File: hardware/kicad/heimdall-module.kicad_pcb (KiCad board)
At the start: 2 copper layers, 54.9 x 30.1 mm, 28 parts

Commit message: Sync the imported PCB with the schematic and clean up ERC
After Update PCB from Schematic, the pads were on the new hierarchical
nets (/VCC, /SDA, ...) but tracks, vias and zones kept the old names;
moved them over. Removed EasyEDA's A4 frame symbol and empty Field42
properties. Gave pins real types: passives, connectors and diode are
passive, MC33269 Vin/Vout are power in/out, ESP32 IOs bidirectional.
GND is now a KiCad power symbol. ERC is down from 100 to 19 and DRC from
167 to 92; what is left is design and layout, not import.

Co-Authored-By: Claude Opus 5.5 <noreply@anthropic.com>
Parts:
- C1: value (none) -> 330nF
- C2: value (none) -> 10uF
- C3, C4: value (none) -> 100nF
- D1: value (none) -> 1N5819
- H1: value (none) -> BG125-05-A-1-1-0440-N-D
- R1, R2: value (none) -> 5.1kΩ
- R10, R8, R9: value (none) -> 10kΩ
- R3, R4: value (none) -> 33Ω
- R5, R6, R7: value (none) -> 220Ω
- U1: value (none) -> MC33269DT-3.3G
- U2: value (none) -> 2.4GHz
- U3: value (none) -> TYPEC-214-ARP14H105
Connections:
- net $1N100 renamed Net-(U2-EN)
- net $1N29 renamed Net-(U3-CC1)
- net $1N37 renamed Net-(U3-CC2)
- net $1N69 renamed Net-(U2-IO19)
- net $1N70 renamed Net-(U2-IO18)
- net $1N77 renamed Net-(U2-IO4)
- net $1N78 renamed Net-(U2-IO5)
- net $1N81 renamed Net-(U2-IO6)
- net DATA renamed /DATA
- net HB renamed /HB
- net IO10 renamed /IO10
- net IO3 renamed /IO3
- net IO7 renamed /IO7
- net RXD renamed /RXD
- net SCL renamed /SCL
- net SDA renamed /SDA
- net SIGNAL renamed /SIGNAL
- net TXD renamed /TXD
- net USB-D+ renamed /USB-D+
- net USB-D- renamed /USB-D-
- net VBAT renamed /VBAT
- net VBUS renamed /VBUS
- net VCC renamed /VCC
- U2 pad 16: (no net) -> unconnected-(U2-IO2-Pad16)
- U2 pad 7: (no net) -> unconnected-(U2-IO8-Pad7)
- U2 pad 8: (no net) -> unconnected-(U2-IO9-Pad8)

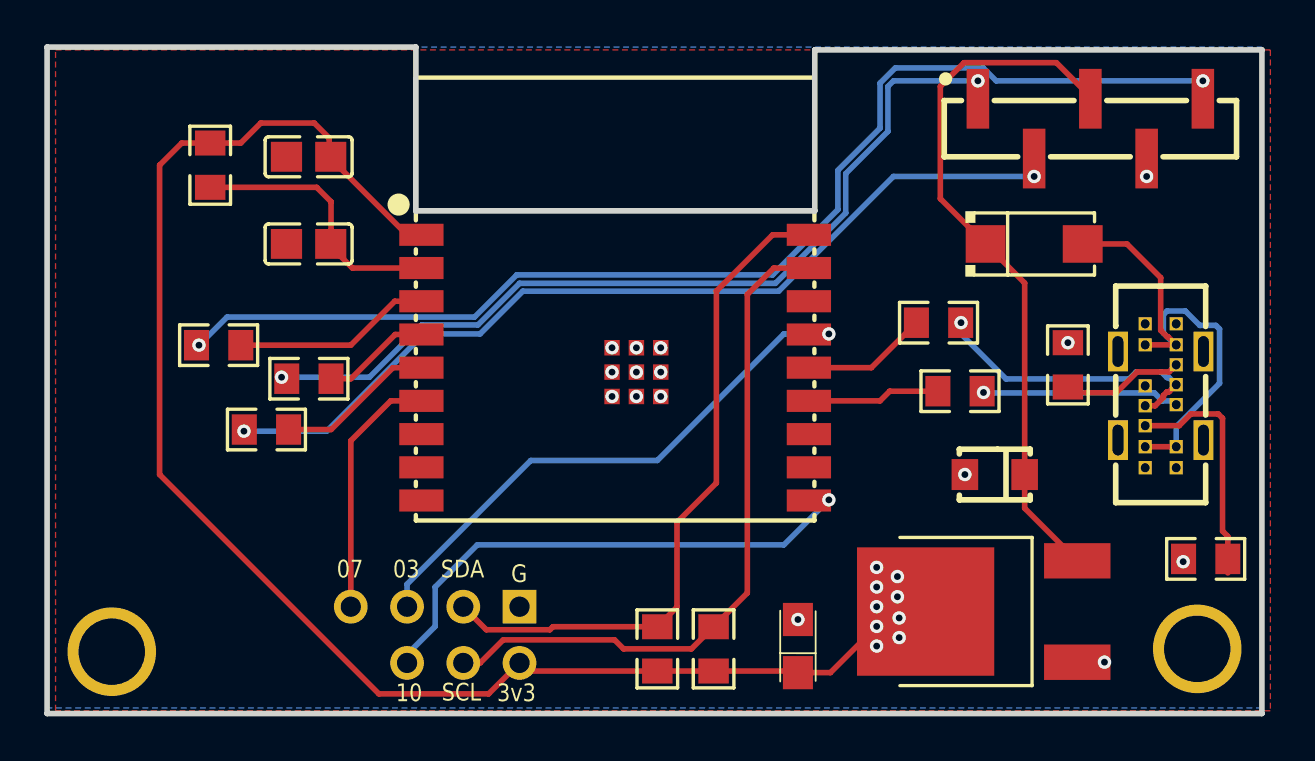
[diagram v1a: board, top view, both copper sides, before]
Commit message: Rev 2: corrected schematic, re-placed and re-routed board
Schematic (on top of the previous commit):
- I2C moved from IO0/IO1 to GPIO20/21 and bay SIGNAL/DATA swapped onto
  IO4/IO5, so the right-hand pins can reach J2 without crossing the 3V3
  trunk. No firmware exists yet. SCL sits on U0TXD (boot log); SDA stays a
  pulled-up input, so no I2C start condition happens at boot. The console
  has to use USB-Serial/JTAG.
- JP1 kept out of BOM/position files; U2 value -> part name.

PCB:
- H1 slot restored: EasyEDA had it as a multi-layer fill (became copper
  in the import). Now a 12.7 x 2.03mm cut-out, H1's pads trimmed to end
  0.5mm before it.
- All copper rebuilt: power class 0.6mm (VBUS, VBAT, VBAT_IN), 3V3 trunk
  0.5mm (Espressif: >= 20 mil), signals 0.25mm, 0.2mm clearance,
  0.7/0.3 and 0.8/0.4 vias. No via touches a pad (checked).
- U1 tab heatsink copper on both layers, vias beside the tab, not in it.
- No tracks/vias on top under the module body (GND only).
- Vertical USB-C: round 0.7mm pads (0.6mm square gave a 0.09mm ring);
  the pin field (VBUS, CC, D+/D- crossover) laid by hand.
- GND pours on both layers, stitched; a GND track along the module's
  bottom pad row joins the right-hand side to the rest.
- Edited footprints written back to the project library.
- route_pcb.py (adapted from heimdall-switch) and rev_pcb.py record how it
  was made.

ERC 0. DRC 0 errors, 0 unconnected, 0 parity; 1 warning (U3 A1 thermal
relief on top has one spoke; the pad also joins the bottom pour).

Co-Authored-By: Claude Opus 5.5 <noreply@anthropic.com>
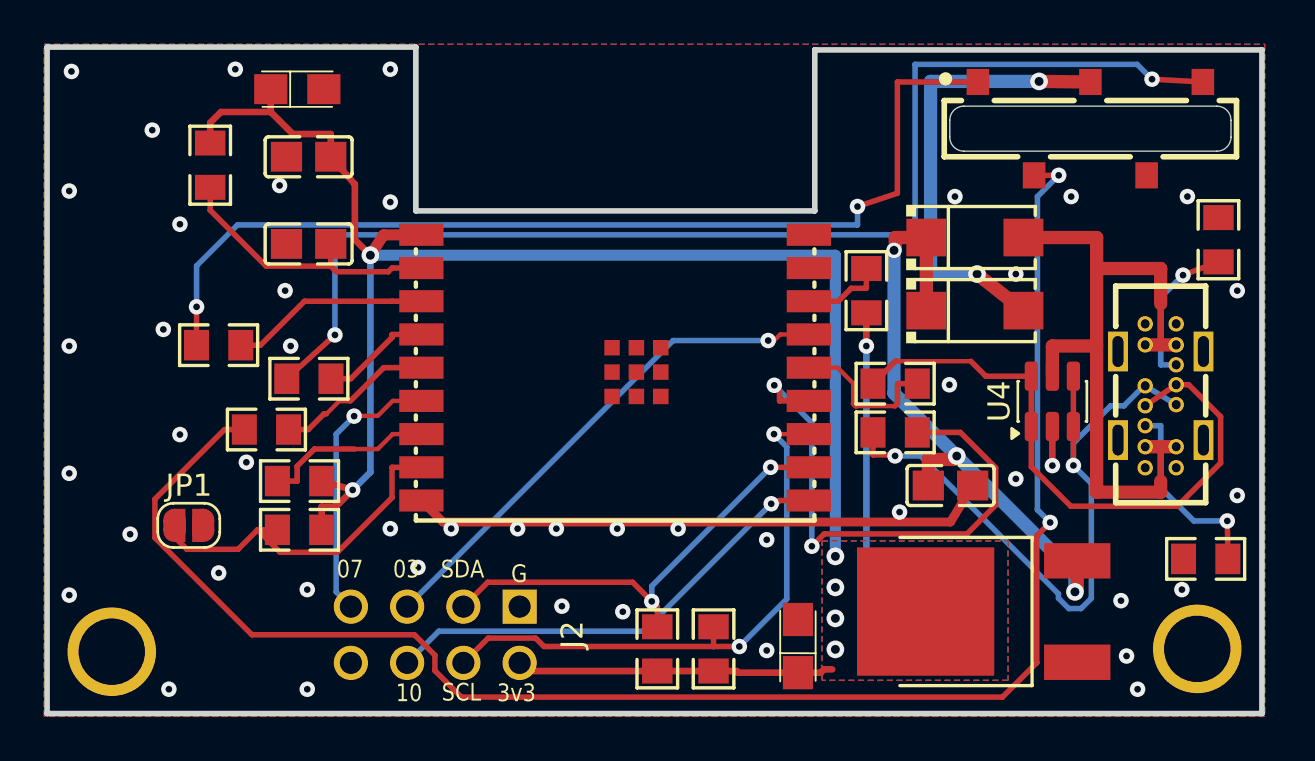
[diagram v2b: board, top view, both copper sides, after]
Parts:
- removed ?: , Pad_e209
- removed ?: , Pad_e211
- removed ?: , Pad_e210
- removed ?: , Pad_e207
- removed ?: , Pad_e206
- removed ?: , Pad_e212
- removed ?: , Pad_e208
- added C5: 10uF, heimdall-m-easyedapro:CASE-A_3216, F.Cu at (131.3, 91.9)
- added D2: 1N5819, heimdall-m-easyedapro:SMA_L4.4-W2.6-LS5.0-RD, F.Cu at (161.9, 101.9)
- added J2: Breakout, Connector_PinHeader_2.54mm:PinHeader_2x04_P2.54mm_Vertical, F.Cu at (141.3, 115.3)
- added JP1: BOOT, Jumper:SolderJumper-2_P1.3mm_Open_RoundedPad1.0x1.5mm, F.Cu at (126.4, 111.6)
- added R11: 10kΩ, heimdall-m-easyedapro:R0805, F.Cu at (157.0, 101.0)
- added R12: 10kΩ, heimdall-m-easyedapro:R0805, F.Cu at (131.4, 109.6)
- added R13: 10kΩ, heimdall-m-easyedapro:R0805, F.Cu at (131.4, 111.8)
- added U4: USBLC6-2SC6, Package_TO_SOT_SMD:SOT-23-6, F.Cu at (165.4, 106.0)
- C1: value 330nF -> 1uF; footprint heimdall-m-easyedapro:CAP-SMD_L3.2-W1.6 -> heimdall-m-easyedapro:C0805
- C4: value 100nF -> 1uF
- U2: value 2.4GHz -> ESP32-C3-WROOM-02-N4
- moved R1 8.84 mm to (172.9, 98.7)
- moved R4 3.47 mm to (158.3, 107.4), turned to 0 degrees
- moved R3 3.38 mm to (158.3, 105.2), turned to 0 degrees
- moved D1 2.69 mm to (161.9, 98.6)
- moved C1 2.06 mm to (160.8, 109.8), turned to 0 degrees
- gave numbers to parts that had none: 2
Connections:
- H1 pad 3: /VBAT -> /VBAT_IN
- R5 pad 1: /DATA -> /SIGNAL
- R6 pad 1: /SIGNAL -> /DATA
- U2 pad 11: /RXD -> /SDA
- U2 pad 12: /TXD -> /SCL
- U2 pad 16: unconnected-(U2-IO2-Pad16) -> /IO2
- U2 pad 17: /SCL -> unconnected-(U2-IO1-Pad17)
- U2 pad 18: /SDA -> unconnected-(U2-IO0-Pad18)
- U2 pad 7: unconnected-(U2-IO8-Pad7) -> /IO8
- U2 pad 8: unconnected-(U2-IO9-Pad8) -> /IO9
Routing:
- net /HB: track 40.5 -> 75.0 mm
- net GND: track 0.00 -> 28.0 mm, vias 15 -> 46
- net /USB-D-: track 8.93 -> 31.4 mm, vias 1 -> 2
- net /VCC: track 69.8 -> 91.7 mm, vias 9 -> 7
- net /VBAT_IN: track 0.00 -> 20.7 mm, vias 0 -> 2
- net Net-(U2-IO18): track 6.01 -> 25.1 mm, vias 0 -> 2
- net /IO9: track 0.00 -> 16.0 mm
- net /USB-D+: track 13.3 -> 28.4 mm, vias 1 -> 0
- net /VBUS: track 21.0 -> 32.3 mm
- net /SDA: track 30.7 -> 20.6 mm, vias 0 -> 2
- net /IO8: track 0.00 -> 7.78 mm
- net /SIGNAL: track 39.2 -> 45.6 mm
- net /SCL: track 31.2 -> 26.3 mm, vias 0 -> 2
- net /VBAT: track 31.8 -> 28.1 mm, vias 0 -> 3
- net /IO2: track 0.00 -> 3.73 mm
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- added copper zone on B.Cu, net /VCC
- added copper zone on F.Cu, net /VCC
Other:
- outline, holes or cut-outs redrawn
